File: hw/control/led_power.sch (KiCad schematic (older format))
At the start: 19 parts, among them Q1001 BC807, Q1002 BC817, U801 LM2678T-ADJ

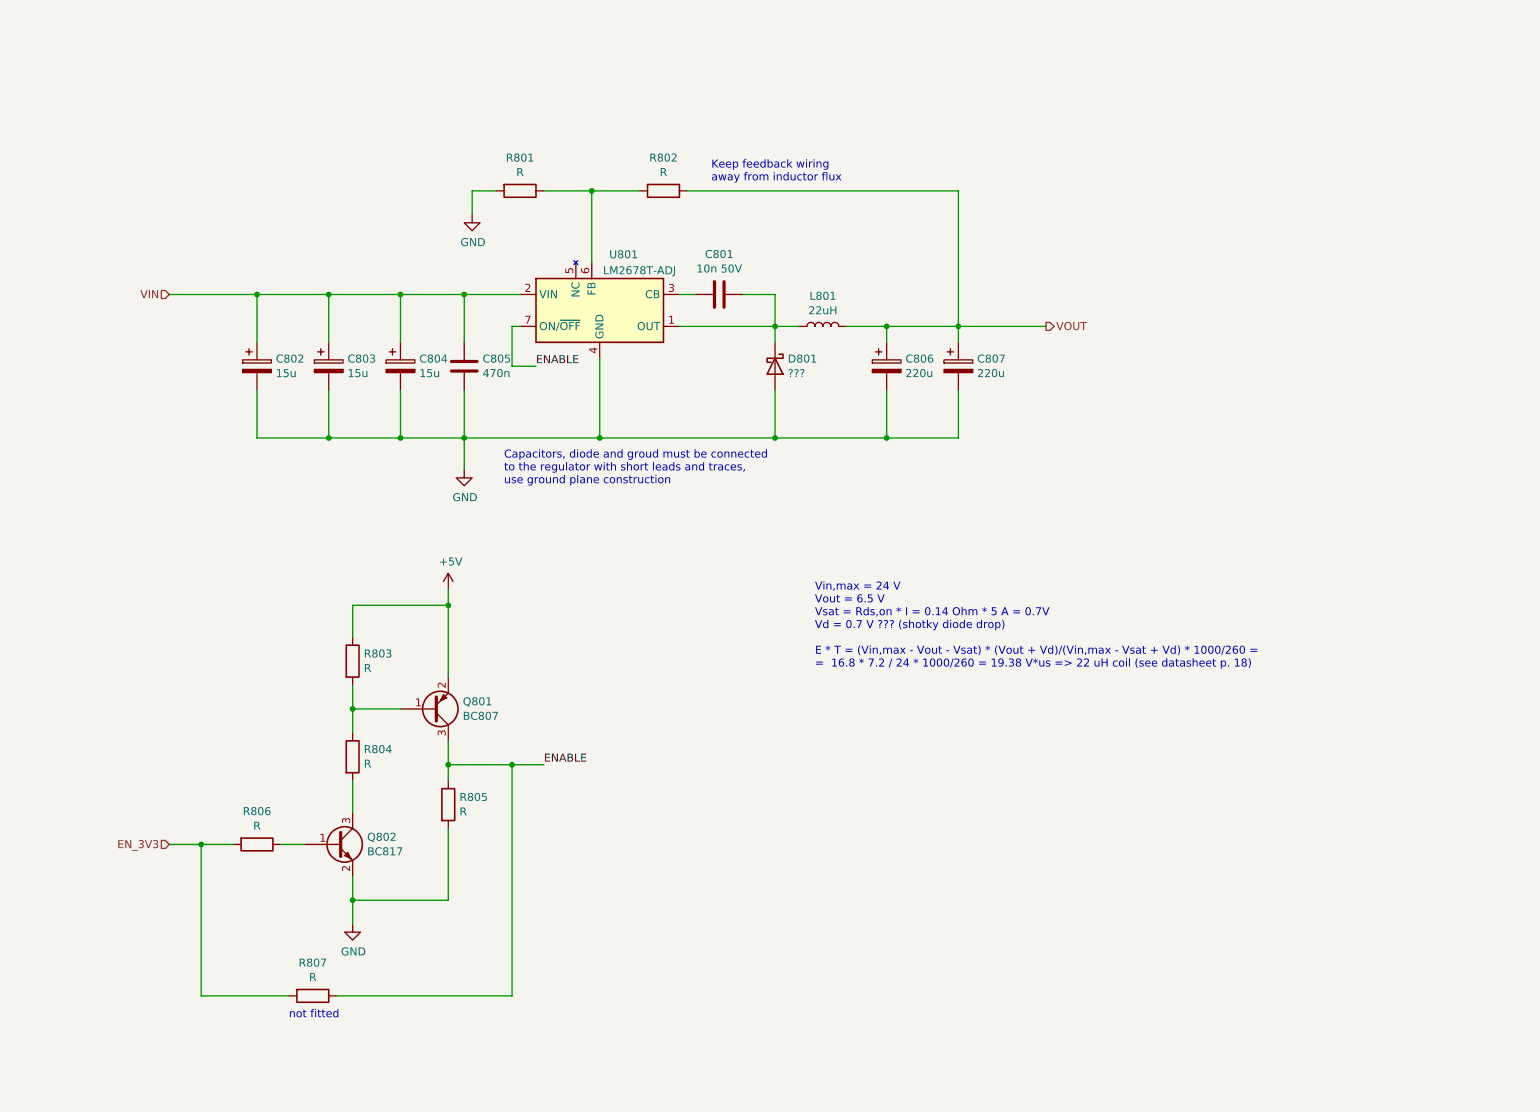
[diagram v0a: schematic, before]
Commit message: [hw] Assign control board footprints
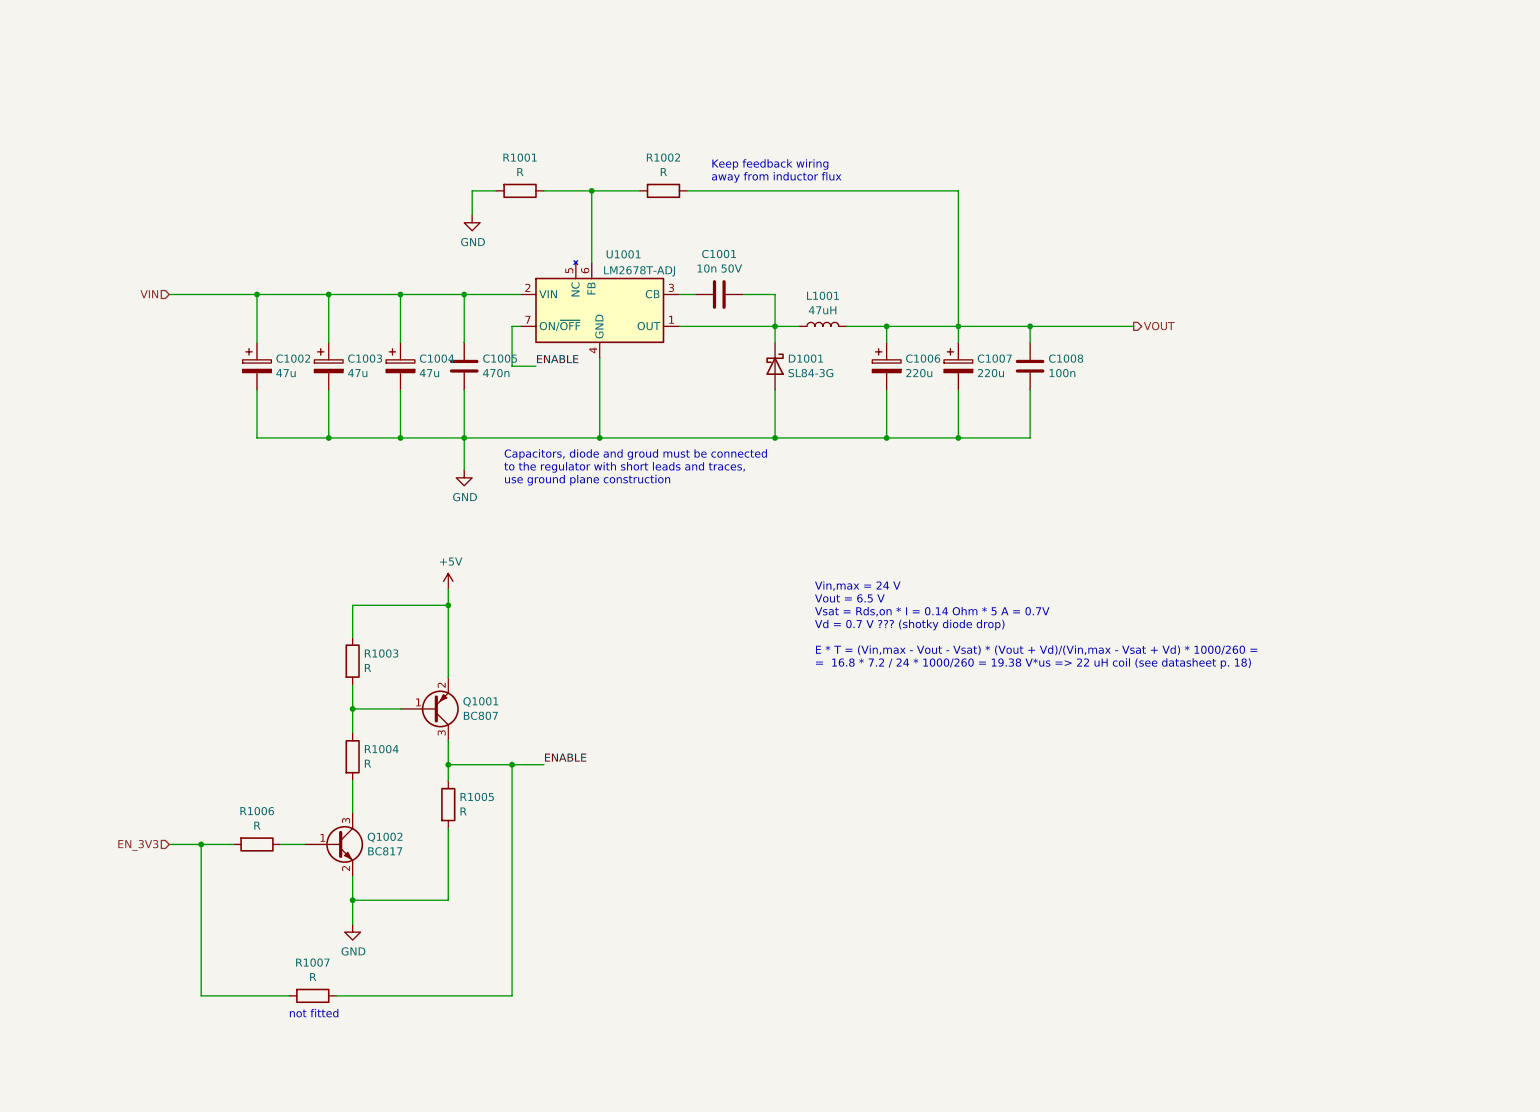
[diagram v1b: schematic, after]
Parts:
- added C808: 100n, Capacitor_SMD:C_0805_2012Metric_Pad1.18x1.45mm_HandSolder, symbol Device:C
- C1002, C1003, C1004: value 15u -> 47u; footprint (none) -> Capacitor_THT:CP_Radial_D8.0mm_P3.50mm
- C1006, C1007: footprint (none) -> Capacitor_THT:CP_Radial_D8.0mm_P3.50mm
- D1001: value ??? -> SL84-3G
- L1001: value 22uH -> 47uH
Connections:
- net GND: now also C808.2
- net VOUT: now also C808.1
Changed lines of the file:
@@
 $Descr A4 11693 8268
 encoding utf-8
-Sheet 8 13
+Sheet 10 13
 Title "WS2812 Controller"
 Date "2021-10-10"
@@
 Text HLabel 2700 5750 0    50   Input ~ 0
 EN_3V3
-Text HLabel 8200 2500 2    50   Output ~ 0
+Text HLabel 8750 2500 2    50   Output ~ 0
 VOUT
 $Comp
@@
 AR Path="/614AB031/6145ECF0" Ref="U801"  Part="1"
 AR Path="/614AE8DA/6145ECF0" Ref="U1001"  Part="1"
-F 0 "U801" H 5550 2750 50  0000 C CNN
+F 0 "U1001" H 5550 2750 50  0000 C CNN
 F 1 "LM2678T-ADJ" H 5650 2650 50  0000 C CNN
 F 2 "Package_TO_SOT_THT:TO-220-7_P2.54x3.7mm_StaggerOdd_Lead3.8mm_Vertical" H 5450 2150 50  0001 L CIN
@@
 AR Path="/614AB031/6145FC0F" Ref="C801"  Part="1"
 AR Path="/614AE8DA/6145FC0F" Ref="C1001"  Part="1"
-F 0 "C801" V 5898 2300 50  0000 C CNN
+F 0 "C1001" V 5898 2300 50  0000 C CNN
 F 1 "10n 50V" V 5989 2300 50  0000 C CNN
 F 2 "Capacitor_SMD:C_0805_2012Metric_Pad1.18x1.45mm_HandSolder" H 6188 2150 50  0001 C CNN
@@
 AR Path="/614AB031/61460B18" Ref="#PWR0802"  Part="1"
 AR Path="/614AE8DA/61460B18" Ref="#PWR01002"  Part="1"
-F 0 "#PWR0802" H 4550 3150 50  0001 C CNN
+F 0 "#PWR01002" H 4550 3150 50  0001 C CNN
 F 1 "GND" H 4555 3227 50  0000 C CNN
 F 2 "" H 4550 3400 50  0001 C CNN
@@
 AR Path="/614AE8DA/61461C6E" Ref="D1001"  Part="1"
 AR Path="/614AB031/61461C6E" Ref="D801"  Part="1"
-F 0 "D801" V 6454 2830 50  0000 L CNN
-F 1 "???" V 6545 2830 50  0000 L CNN
+F 0 "D1001" V 6454 2830 50  0000 L CNN
+F 1 "SL84-3G" V 6545 2830 50  0000 L CNN
 F 2 "Diode_SMD:D_SMC_Handsoldering" H 6500 2750 50  0001 C CNN
 F 3 "~" H 6500 2750 50  0001 C CNN
@@
 AR Path="/614AE8DA/61462D51" Ref="L1001"  Part="1"
 AR Path="/614AB031/61462D51" Ref="L801"  Part="1"
-F 0 "L801" V 6990 2500 50  0000 C CNN
-F 1 "22uH" V 6899 2500 50  0000 C CNN
+F 0 "L1001" V 6990 2500 50  0000 C CNN
+F 1 "47uH" V 6899 2500 50  0000 C CNN
 F 2 "Inductor_THT:L_Toroid_Vertical_L22.4mm_W10.2mm_P7.90mm_Vishay_TJ4" H 6800 2500 50  0001 C CNN
 F 3 "~" H 6800 2500 50  0001 C CNN
@@
 AR Path="/614AE8DA/61463CC3" Ref="C1006"  Part="1"
 AR Path="/614AB031/61463CC3" Ref="C806"  Part="1"
-F 0 "C806" H 7318 2796 50  0000 L CNN
+F 0 "C1006" H 7318 2796 50  0000 L CNN
 F 1 "220u" H 7318 2705 50  0000 L CNN
-F 2 "" H 7238 2600 50  0001 C CNN
+F 2 "Capacitor_THT:CP_Radial_D8.0mm_P3.50mm" H 7238 2600 50  0001 C CNN
 F 3 "~" H 7200 2750 50  0001 C CNN
 	1    7200 2750
@@
 AR Path="/614AE8DA/6146511A" Ref="C1007"  Part="1"
 AR Path="/614AB031/6146511A" Ref="C807"  Part="1"
-F 0 "C807" H 7768 2796 50  0000 L CNN
+F 0 "C1007" H 7768 2796 50  0000 L CNN
 F 1 "220u" H 7768 2705 50  0000 L CNN
-F 2 "" H 7688 2600 50  0001 C CNN
+F 2 "Capacitor_THT:CP_Radial_D8.0mm_P3.50mm" H 7688 2600 50  0001 C CNN
 F 3 "~" H 7650 2750 50  0001 C CNN
 	1    7650 2750
@@
 AR Path="/614AE8DA/61465477" Ref="C1004"  Part="1"
 AR Path="/614AB031/61465477" Ref="C804"  Part="1"
-F 0 "C804" H 4268 2796 50  0000 L CNN
-F 1 "15u" H 4268 2705 50  0000 L CNN
-F 2 "" H 4188 2600 50  0001 C CNN
+F 0 "C1004" H 4268 2796 50  0000 L CNN
+F 1 "47u" H 4268 2705 50  0000 L CNN
+F 2 "Capacitor_THT:CP_Radial_D8.0mm_P3.50mm" H 4188 2600 50  0001 C CNN
 F 3 "~" H 4150 2750 50  0001 C CNN
 	1    4150 2750
@@
 AR Path="/614AE8DA/614679D1" Ref="C1003"  Part="1"
 AR Path="/614AB031/614679D1" Ref="C803"  Part="1"
-F 0 "C803" H 3818 2796 50  0000 L CNN
-F 1 "15u" H 3818 2705 50  0000 L CNN
-F 2 "" H 3738 2600 50  0001 C CNN
+F 0 "C1003" H 3818 2796 50  0000 L CNN
+F 1 "47u" H 3818 2705 50  0000 L CNN
+F 2 "Capacitor_THT:CP_Radial_D8.0mm_P3.50mm" H 3738 2600 50  0001 C CNN
 F 3 "~" H 3700 2750 50  0001 C CNN
 	1    3700 2750
@@
 AR Path="/614AE8DA/61467CFC" Ref="C1002"  Part="1"
 AR Path="/614AB031/61467CFC" Ref="C802"  Part="1"
-F 0 "C802" H 3368 2796 50  0000 L CNN
-F 1 "15u" H 3368 2705 50  0000 L CNN
-F 2 "" H 3288 2600 50  0001 C CNN
+F 0 "C1002" H 3368 2796 50  0000 L CNN
+F 1 "47u" H 3368 2705 50  0000 L CNN
+F 2 "Capacitor_THT:CP_Radial_D8.0mm_P3.50mm" H 3288 2600 50  0001 C CNN
 F 3 "~" H 3250 2750 50  0001 C CNN
 	1    3250 2750
@@
 AR Path="/614AE8DA/614681BF" Ref="C1005"  Part="1"
 AR Path="/614AB031/614681BF" Ref="C805"  Part="1"
-F 0 "C805" H 4665 2796 50  0000 L CNN
+F 0 "C1005" H 4665 2796 50  0000 L CNN
 F 1 "470n" H 4665 2705 50  0000 L CNN
 F 2 "Capacitor_SMD:C_0805_2012Metric_Pad1.18x1.45mm_HandSolder" H 4588 2600 50  0001 C CNN
@@
 	7650 3200 7650 2900
 Wire Wire Line
-	7650 2500 8200 2500
+	7650 2500 8100 2500
 Connection ~ 7650 2500
 $Comp
@@
 AR Path="/614AE8DA/6147393D" Ref="R1002"  Part="1"
 AR Path="/614AB031/6147393D" Ref="R802"  Part="1"
-F 0 "R802" V 5593 1650 50  0000 C CNN
+F 0 "R1002" V 5593 1650 50  0000 C CNN
 F 1 "R" V 5684 1650 50  0000 C CNN
 F 2 "Resistor_SMD:R_0805_2012Metric_Pad1.20x1.40mm_HandSolder" V 5730 1650 50  0001 C CNN
@@
 AR Path="/614AE8DA/61475A47" Ref="R1001"  Part="1"
 AR Path="/614AB031/61475A47" Ref="R801"  Part="1"
-F 0 "R801" V 4693 1650 50  0000 C CNN
+F 0 "R1001" V 4693 1650 50  0000 C CNN
 F 1 "R" V 4784 1650 50  0000 C CNN
 F 2 "Resistor_SMD:R_0805_2012Metric_Pad1.20x1.40mm_HandSolder" V 4830 1650 50  0001 C CNN
@@
 AR Path="/614AE8DA/61477A40" Ref="#PWR01001"  Part="1"
 AR Path="/614AB031/61477A40" Ref="#PWR0801"  Part="1"
-F 0 "#PWR0801" H 4600 1550 50  0001 C CNN
+F 0 "#PWR01001" H 4600 1550 50  0001 C CNN
 F 1 "GND" H 4605 1627 50  0000 C CNN
 F 2 "" H 4600 1800 50  0001 C CNN
@@
 AR Path="/614AE8DA/6147DB7E" Ref="R1006"  Part="1"
 AR Path="/614AB031/6147DB7E" Ref="R806"  Part="1"
-F 0 "R806" V 3043 5750 50  0000 C CNN
+F 0 "R1006" V 3043 5750 50  0000 C CNN
 F 1 "R" V 3134 5750 50  0000 C CNN
 F 2 "Resistor_SMD:R_0805_2012Metric_Pad1.20x1.40mm_HandSolder" V 3180 5750 50  0001 C CNN
@@
 AR Path="/614AE8DA/6147EFCD" Ref="Q1002"  Part="1"
 AR Path="/614AB031/6147EFCD" Ref="Q802"  Part="1"
-F 0 "Q802" H 3941 5796 50  0000 L CNN
+F 0 "Q1002" H 3941 5796 50  0000 L CNN
 F 1 "BC817" H 3941 5705 50  0000 L CNN
 F 2 "Package_TO_SOT_SMD:SOT-23_Handsoldering" H 3950 5850 50  0001 C CNN
@@
 AR Path="/614AE8DA/61480A0D" Ref="Q1001"  Part="1"
 AR Path="/614AB031/61480A0D" Ref="Q801"  Part="1"
-F 0 "Q801" H 4541 4854 50  0000 L CNN
+F 0 "Q1001" H 4541 4854 50  0000 L CNN
 F 1 "BC807" H 4541 4945 50  0000 L CNN
 F 2 "Package_TO_SOT_SMD:SOT-23_Handsoldering" H 4550 5000 50  0001 C CNN
@@
 AR Path="/614AE8DA/6148128F" Ref="R1004"  Part="1"
 AR Path="/614AB031/6148128F" Ref="R804"  Part="1"
-F 0 "R804" H 3920 5246 50  0000 L CNN
+F 0 "R1004" H 3920 5246 50  0000 L CNN
 F 1 "R" H 3920 5155 50  0000 L CNN
 F 2 "Resistor_SMD:R_0805_2012Metric_Pad1.20x1.40mm_HandSolder" V 3780 5200 50  0001 C CNN
@@
 AR Path="/614AE8DA/614817B0" Ref="R1003"  Part="1"
 AR Path="/614AB031/614817B0" Ref="R803"  Part="1"
-F 0 "R803" H 3920 4646 50  0000 L CNN
+F 0 "R1003" H 3920 4646 50  0000 L CNN
 F 1 "R" H 3920 4555 50  0000 L CNN
 F 2 "Resistor_SMD:R_0805_2012Metric_Pad1.20x1.40mm_HandSolder" V 3780 4600 50  0001 C CNN
@@
 AR Path="/614AE8DA/61483286" Ref="#PWR01004"  Part="1"
 AR Path="/614AB031/61483286" Ref="#PWR0804"  Part="1"
-F 0 "#PWR0804" H 3850 6000 50  0001 C CNN
+F 0 "#PWR01004" H 3850 6000 50  0001 C CNN
 F 1 "GND" H 3855 6077 50  0000 C CNN
 F 2 "" H 3850 6250 50  0001 C CNN
@@
 AR Path="/614AE8DA/61486663" Ref="#PWR01003"  Part="1"
 AR Path="/614AB031/61486663" Ref="#PWR0803"  Part="1"
-F 0 "#PWR0803" H 4450 4000 50  0001 C CNN
+F 0 "#PWR01003" H 4450 4000 50  0001 C CNN
 F 1 "+5V" H 4465 4323 50  0000 C CNN
 F 2 "" H 4450 4150 50  0001 C CNN
@@
 AR Path="/614AE8DA/6148D73D" Ref="R1005"  Part="1"
 AR Path="/614AB031/6148D73D" Ref="R805"  Part="1"
-F 0 "R805" H 4520 5546 50  0000 L CNN
+F 0 "R1005" H 4520 5546 50  0000 L CNN
 F 1 "R" H 4520 5455 50  0000 L CNN
 F 2 "Resistor_SMD:R_0805_2012Metric_Pad1.20x1.40mm_HandSolder" V 4380 5500 50  0001 C CNN
@@
 AR Path="/614AE8DA/614CC1BE" Ref="R1007"  Part="1"
 AR Path="/614AB031/614CC1BE" Ref="R807"  Part="1"
-F 0 "R807" V 3393 6700 50  0000 C CNN
+F 0 "R1007" V 3393 6700 50  0000 C CNN
 F 1 "R" V 3484 6700 50  0000 C CNN
 F 2 "Resistor_SMD:R_0805_2012Metric_Pad1.20x1.40mm_HandSolder" V 3530 6700 50  0001 C CNN
@@
 Text Notes 6750 4650 0    50   ~ 0
 Vin,max = 24 V\nVout = 6.5 V\nVsat = Rds,on * I = 0.14 Ohm * 5 A = 0.7V\nVd = 0.7 V ??? (shotky diode drop)\n\nE * T = (Vin,max - Vout - Vsat) * (Vout + Vd)/(Vin,max - Vsat + Vd) * 1000/260 = \n=  16.8 * 7.2 / 24 * 1000/260 = 19.38 V*us => 22 uH coil (see datasheet p. 18)
+$Comp
+L Device:C C808
+U 1 1 6169A3CC
+P 8100 2750
+AR Path="/614AB031/6169A3CC" Ref="C808"  Part="1"
+AR Path="/614AE8DA/6169A3CC" Ref="C1008"  Part="1"
+F 0 "C1008" H 8215 2796 50  0000 L CNN
+F 1 "100n" H 8215 2705 50  0000 L CNN
+F 2 "Capacitor_SMD:C_0805_2012Metric_Pad1.18x1.45mm_HandSolder" H 8138 2600 50  0001 C CNN
+F 3 "~" H 8100 2750 50  0001 C CNN
+	1    8100 2750
+	1    0    0    -1
+$EndComp
+Wire Wire Line
+	8100 2600 8100 2500
+Connection ~ 8100 2500
+Wire Wire Line
+	8100 2500 8750 2500
+Wire Wire Line
+	7650 3200 8100 3200
+Wire Wire Line
+	8100 3200 8100 2900
+Connection ~ 7650 3200
 $EndSCHEMATC

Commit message: [hw] Incorporate suggestions
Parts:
- added C809: C, symbol Device:C
- added D?: 1.5KExxA, Diode_THT:D_DO-201AE_P15.24mm_Horizontal, symbol Diode:1.5KExxA
- added D?: D_Schottky, symbol Device:D_Schottky
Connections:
- net GND: now also D?.2 (A2)
- net VIN: now also D?.1 (K)
- net VOUT: now also C809.1, D?.1 (A1), D?.2 (A)
- net at R1001.1, R1002.2, U801.6 (FB): now also C809.2
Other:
- note added: "Alternative\nNot mounted"
- note removed: "not fitted"
- moved on the sheet: R807
